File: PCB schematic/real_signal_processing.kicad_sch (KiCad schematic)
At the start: 18 parts, among them U1 OPA2365AID

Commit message: schematic
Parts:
- C20: footprint Capacitor_THT:C_Rect_L7.0mm_W4.5mm_P5.00mm -> Misc. Footprints:CAP_C330_KEM
- C21, C34, C36, C38: footprint (none) -> Misc. Footprints:CAP_AR20_AVX
- C26, C27, C29: footprint (none) -> Capacitor_SMD:C_0603_1608Metric_Pad1.08x0.95mm_HandSolder
- C28: footprint (none) -> Misc. Footprints:CAP_C330_KEM
- R18, R19, R24, R25, R26: footprint (none) -> Resistor_SMD:R_0603_1608Metric_Pad0.98x0.95mm_HandSolder
- R23: footprint (none) -> Resistor_THT:R_Axial_DIN0204_L3.6mm_D1.6mm_P5.08mm_Horizontal

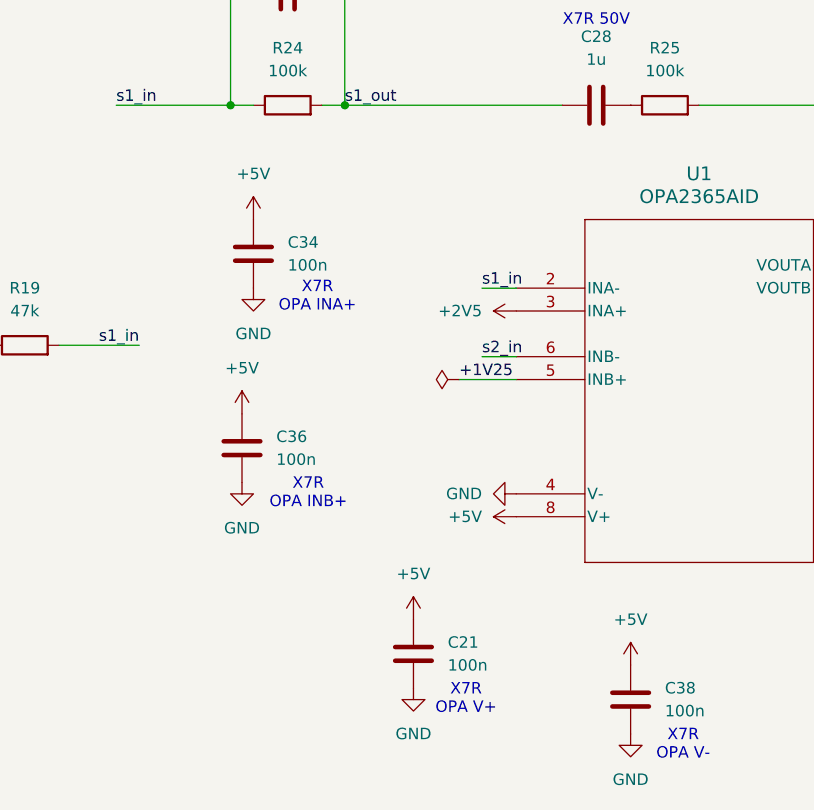
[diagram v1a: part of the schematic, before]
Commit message: schematic layout mostly done
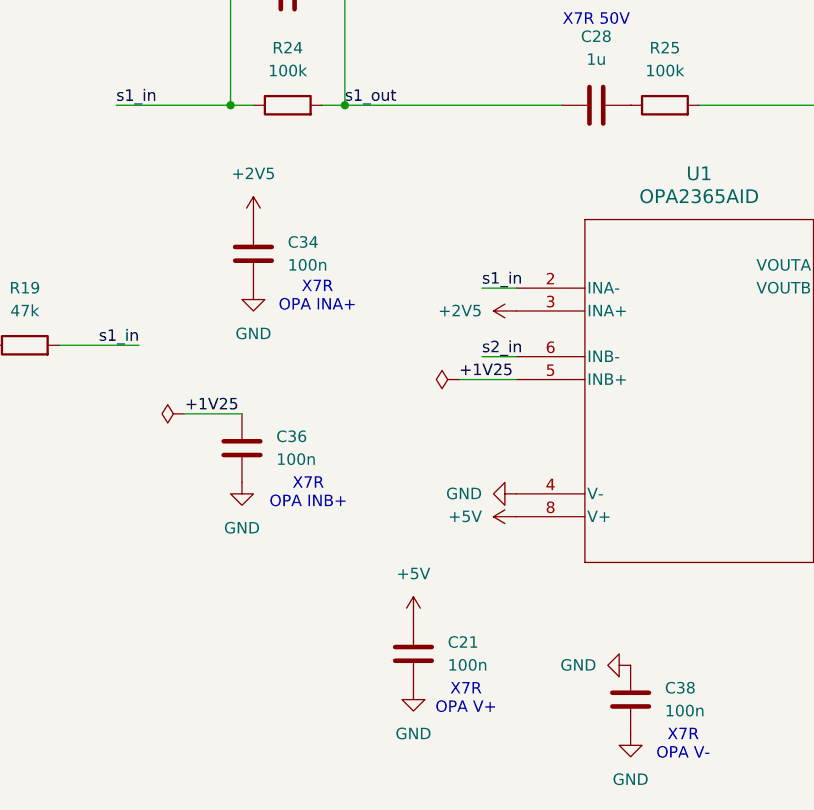
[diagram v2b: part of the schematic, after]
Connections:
- net +2V5: now also C34.1
- net +5V: no longer C34.1, C36.1, C38.1
- net 1V25_IN: now also C36.1
- net GND: now also C38.1

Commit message: pcb initial complete revision
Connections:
- net ac_coupled: now also D3.2 (A), D5.1 (K)
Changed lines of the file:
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@@
+	)
+	(junction
+		(at 72.39 128.27)
+		(diameter 0)
+		(color 0 0 0 0)
 	)
 	(junction
@@
 	(wire
 		(pts
+			(xy 72.39 128.27) (xy 72.39 130.81)
+		)
+		(stroke
+			(width 0)
+			(type default)
+		)
+	)
+	(wire
+		(pts
 			(xy 160.02 101.6) (xy 186.69 101.6)
 		)
@@
 	(wire
 		(pts
-			(xy 63.5 128.27) (xy 81.28 128.27)
+			(xy 63.5 128.27) (xy 72.39 128.27)
 		)
 		(stroke
@@
 	(wire
 		(pts
+			(xy 72.39 128.27) (xy 81.28 128.27)
+		)
+		(stroke
+			(width 0)
+			(type default)
+		)
+	)
+	(wire
+		(pts
 			(xy 199.39 101.6) (xy 196.85 101.6)
 		)
@@
 	(wire
 		(pts
-			(xy 72.39 125.73) (xy 72.39 130.81)
-		)
-		(stroke
+			(xy 72.39 125.73) (xy 72.39 128.27)
+		)
+		(stroke
